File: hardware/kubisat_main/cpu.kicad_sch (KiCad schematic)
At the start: 0 parts

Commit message: added MCU based on arduino zeros ATSAMD21G18A
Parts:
- added U1: ATSAMD21G18A-A, Package_QFP:TQFP-48_7x7mm_P0.5mm, symbol MCU_Microchip_SAMD:ATSAMD21G18A-A
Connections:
- new net: U1.18 (GND), U1.35 (GND), U1.42 (GND)
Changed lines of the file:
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@@
 	(generator_version "8.0")
 	(paper "A4")
+	(symbol
+		(lib_id "MCU_Microchip_SAMD:ATSAMD21G18A-A")
+		(at 81.28 102.87 180)
+		(unit 1)
+		(exclude_from_sim no)
+		(in_bom yes)
+		(on_board yes)
+		(dnp no)
+		(fields_autoplaced yes)
+		(property "Reference" "U1"
+			(at 84.2965 52.07 0)
+			(effects
+				(font
+					(size 1.27 1.27)
+				)
+				(justify right)
+			)
+		)
+		(property "Value" "ATSAMD21G18A-A"
+			(at 84.2965 54.61 0)
+			(effects
+				(font
+					(size 1.27 1.27)
+				)
+				(justify right)
+			)
+		)
+		(property "Footprint" "Package_QFP:TQFP-48_7x7mm_P0.5mm"
+			(at 58.42 55.88 0)
+			(effects
+				(font
+					(size 1.27 1.27)
+				)
+				(hide yes)
+			)
+		)
+		(property "Datasheet" "http://ww1.microchip.com/downloads/en/DeviceDoc/SAM_D21_DA1_Family_Data%20Sheet_DS40001882E.pdf"
+			(at 81.28 128.27 0)
+			(effects
+				(font
+					(size 1.27 1.27)
+				)
+				(hide yes)
+			)
+		)
+		(property "Description" "SAM D21 Microchip SMART ARM-based Flash MCU, 48Mhz, 256K Flash, 32K SRAM, TQFP-48"
+			(at 81.28 102.87 0)
+			(effects
+				(font
+					(size 1.27 1.27)
+				)
+				(hide yes)
+			)
+		)
+		(pin "16"
+		)
+		(pin "14"
+		)
+		(pin "23"
+		)
+		(pin "45"
+		)
+		(pin "7"
+		)
+		(pin "33"
+		)
+		(pin "35"
+		)
+		(pin "46"
+		)
+		(pin "47"
+		)
+		(pin "8"
+		)
+		(pin "19"
+		)
+		(pin "2"
+		)
+		(pin "39"
+		)
+		(pin "27"
+		)
+		(pin "32"
+		)
+		(pin "44"
+		)
+		(pin "3"
+		)
+		(pin "1"
+		)
+		(pin "34"
+		)
+		(pin "40"
+		)
+		(pin "24"
+		)
+		(pin "26"
+		)
+		(pin "36"
+		)
+		(pin "18"
+		)
+		(pin "37"
+		)
+		(pin "31"
+		)
+		(pin "4"
+		)
+		(pin "20"
+		)
+		(pin "17"
+		)
+		(pin "5"
+		)
+		(pin "22"
+		)
+		(pin "28"
+		)
+		(pin "42"
+		)
+		(pin "15"
+		)
+		(pin "29"
+		)
+		(pin "6"
+		)
+		(pin "25"
+		)
+		(pin "30"
+		)
+		(pin "21"
+		)
+		(pin "48"
+		)
+		(pin "38"
+		)
+		(pin "10"
+		)
+		(pin "9"
+		)
+		(pin "41"
+		)
+		(pin "43"
+		)
+		(pin "11"
+		)
+		(pin "12"
+		)
+		(pin "13"
+		)
+		(instances
+			(project ""
+				(path "/8e012760-7134-459b-b212-1cb69dd2e1ec/2c7d03ec-a54e-4ab4-a35e-dcb69dfe6e0e"
+					(reference "U1")
+					(unit 1)
+				)
+			)
+		)
+	)
 )

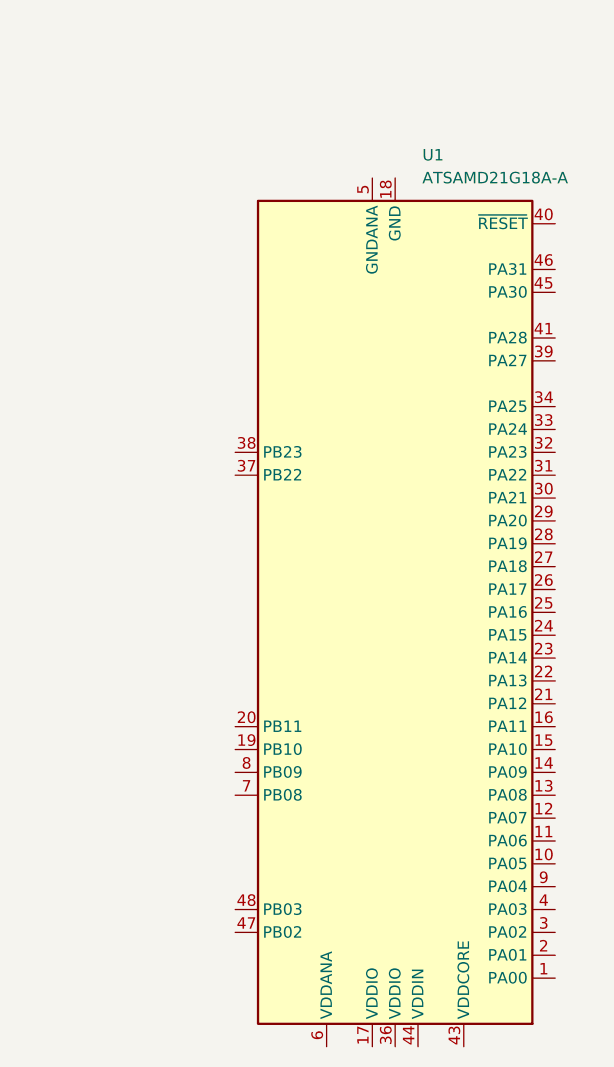
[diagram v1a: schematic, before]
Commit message: added arduino code, more items on main schematic
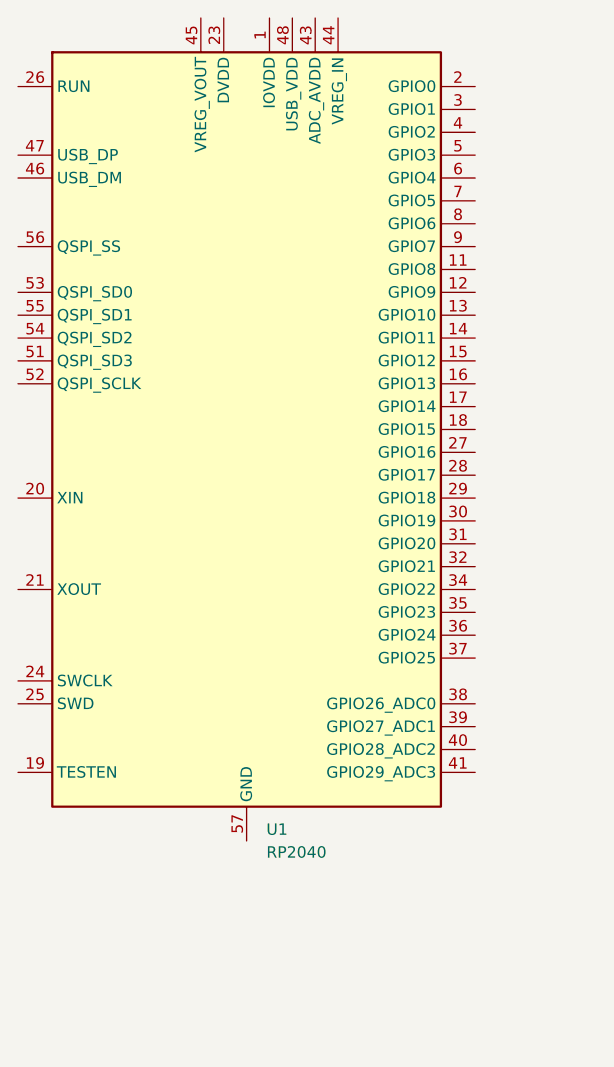
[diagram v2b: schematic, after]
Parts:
- removed U1: ATSAMD21G18A-A, Package_QFP:TQFP-48_7x7mm_P0.5mm, symbol MCU_Microchip_SAMD:ATSAMD21G18A-A
- added U1: RP2040, Package_DFN_QFN:QFN-56-1EP_7x7mm_P0.4mm_EP3.2x3.2mm, symbol MCU_RaspberryPi:RP2040
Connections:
- new net: U1.1 (IOVDD), U1.10 (IOVDD), U1.22 (IOVDD), U1.33 (IOVDD), U1.42 (IOVDD), U1.49 (IOVDD)
- new net: U1.23 (DVDD), U1.50 (DVDD)
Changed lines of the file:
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@@
 	(paper "A4")
 	(symbol
-		(lib_id "MCU_Microchip_SAMD:ATSAMD21G18A-A")
-		(at 81.28 102.87 180)
+		(lib_id "MCU_RaspberryPi:RP2040")
+		(at 64.77 82.55 0)
 		(unit 1)
 		(exclude_from_sim no)
@@
 		(fields_autoplaced yes)
 		(property "Reference" "U1"
-			(at 84.2965 52.07 0)
+			(at 66.9641 127 0)
 			(effects
 				(font
 					(size 1.27 1.27)
 				)
-				(justify right)
+				(justify left)
 			)
 		)
-		(property "Value" "ATSAMD21G18A-A"
-			(at 84.2965 54.61 0)
+		(property "Value" "RP2040"
+			(at 66.9641 129.54 0)
 			(effects
 				(font
 					(size 1.27 1.27)
 				)
-				(justify right)
+				(justify left)
 			)
 		)
-		(property "Footprint" "Package_QFP:TQFP-48_7x7mm_P0.5mm"
-			(at 58.42 55.88 0)
+		(property "Footprint" "Package_DFN_QFN:QFN-56-1EP_7x7mm_P0.4mm_EP3.2x3.2mm"
+			(at 64.77 82.55 0)
 			(effects
 				(font
@@
 			)
 		)
-		(property "Datasheet" "http://ww1.microchip.com/downloads/en/DeviceDoc/SAM_D21_DA1_Family_Data%20Sheet_DS40001882E.pdf"
-			(at 81.28 128.27 0)
+		(property "Datasheet" "https://datasheets.raspberrypi.com/rp2040/rp2040-datasheet.pdf"
+			(at 64.77 82.55 0)
 			(effects
 				(font
@@
 			)
 		)
-		(property "Description" "SAM D21 Microchip SMART ARM-based Flash MCU, 48Mhz, 256K Flash, 32K SRAM, TQFP-48"
-			(at 81.28 102.87 0)
+		(property "Description" "A microcontroller by Raspberry Pi"
+			(at 64.77 82.55 0)
 			(effects
 				(font
@@
 			)
 		)
-		(pin "16"
+		(pin "15"
 		)
 		(pin "14"
 		)
-		(pin "23"
+		(pin "25"
+		)
+		(pin "27"
+		)
+		(pin "3"
+		)
+		(pin "32"
+		)
+		(pin "1"
+		)
+		(pin "4"
+		)
+		(pin "43"
 		)
 		(pin "45"
-		)
-		(pin "7"
-		)
-		(pin "33"
-		)
-		(pin "35"
 		)
 		(pin "46"
@@
 		(pin "47"
 		)
+		(pin "53"
+		)
+		(pin "13"
+		)
+		(pin "41"
+		)
+		(pin "54"
+		)
+		(pin "30"
+		)
+		(pin "56"
+		)
+		(pin "18"
+		)
+		(pin "57"
+		)
+		(pin "36"
+		)
 		(pin "8"
+		)
+		(pin "50"
+		)
+		(pin "9"
+		)
+		(pin "16"
+		)
+		(pin "23"
+		)
+		(pin "24"
+		)
+		(pin "31"
+		)
+		(pin "44"
+		)
+		(pin "39"
+		)
+		(pin "52"
 		)
 		(pin "19"
 		)
+		(pin "38"
+		)
+		(pin "6"
+		)
+		(pin "7"
+		)
 		(pin "2"
 		)
-		(pin "39"
-		)
-		(pin "27"
-		)
-		(pin "32"
-		)
-		(pin "44"
-		)
-		(pin "3"
-		)
-		(pin "1"
+		(pin "11"
 		)
 		(pin "34"
 		)
+		(pin "42"
+		)
+		(pin "55"
+		)
+		(pin "12"
+		)
+		(pin "20"
+		)
+		(pin "28"
+		)
+		(pin "33"
+		)
+		(pin "48"
+		)
+		(pin "22"
+		)
+		(pin "49"
+		)
 		(pin "40"
 		)
-		(pin "24"
+		(pin "5"
+		)
+		(pin "51"
 		)
 		(pin "26"
 		)
-		(pin "36"
+		(pin "29"
 		)
-		(pin "18"
+		(pin "21"
+		)
+		(pin "17"
 		)
 		(pin "37"
 		)
-		(pin "31"
-		)
-		(pin "4"
-		)
-		(pin "20"
-		)
-		(pin "17"
-		)
-		(pin "5"
-		)
-		(pin "22"
-		)
-		(pin "28"
-		)
-		(pin "42"
-		)
-		(pin "15"
-		)
-		(pin "29"
-		)
-		(pin "6"
-		)
-		(pin "25"
-		)
-		(pin "30"
-		)
-		(pin "21"
-		)
-		(pin "48"
-		)
-		(pin "38"
+		(pin "35"
 		)
 		(pin "10"
 		)
-		(pin "9"
-		)
-		(pin "41"
-		)
-		(pin "43"
-		)
-		(pin "11"
-		)
-		(pin "12"
-		)
-		(pin "13"
-		)
 		(instances

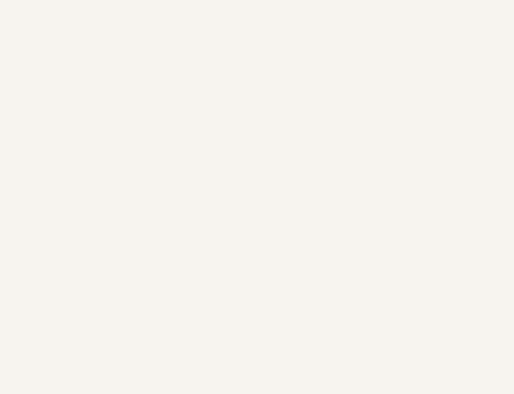
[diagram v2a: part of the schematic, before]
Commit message: added elements and traces to main pcb
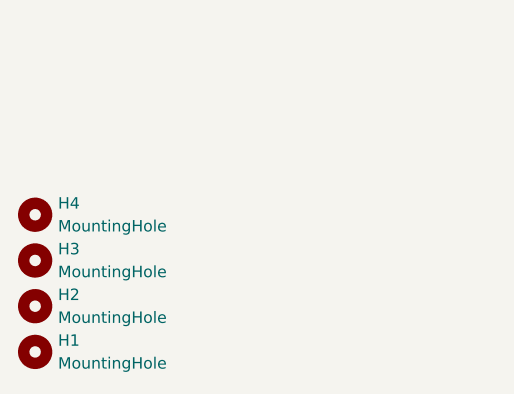
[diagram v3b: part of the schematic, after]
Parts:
- added H1, H2, H3, H4: MountingHole, MountingHole:MountingHole_3.2mm_M3_DIN965, symbol Mechanical:MountingHole

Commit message: added microsd footprint
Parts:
- removed U1: RP2040, Package_DFN_QFN:QFN-56-1EP_7x7mm_P0.4mm_EP3.2x3.2mm, symbol MCU_RaspberryPi:RP2040
- added J2: Micro_SD_Card_Det1, Connector_Card:MR01A-01211, symbol Connector:Micro_SD_Card_Det1
- added J3, J4: Conn_01x08_Socket, Connector_PinHeader_2.54mm:PinHeader_1x08_P2.54mm_Vertical, symbol Connector:Conn_01x08_Socket
- added J5: Conn_01x07_Socket, Connector_PinSocket_2.54mm:PinSocket_1x07_P2.54mm_Vertical, symbol Connector:Conn_01x07_Socket

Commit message: added elements to cpu schematic
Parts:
- removed J3, J4: Conn_01x08_Socket, Connector_PinHeader_2.54mm:PinHeader_1x08_P2.54mm_Vertical, symbol Connector:Conn_01x08_Socket
- removed J5: Conn_01x07_Socket, Connector_PinSocket_2.54mm:PinSocket_1x07_P2.54mm_Vertical, symbol Connector:Conn_01x07_Socket
- added C11, C12, C14, C18, C19, C20, C21, C22, C23, C24, C25: 100n, Capacitor_SMD:C_0805_2012Metric, symbol Device:C
- added C13, C15: 2u2, Capacitor_SMD:C_0805_2012Metric, symbol Device:C
- added C16, C17: 15p, Capacitor_SMD:C_0805_2012Metric, symbol Device:C
- added J3: Conn_01x06_MountingPin, Connector_JST:JST_PH_S6B-PH-SM4-TB_1x06-1MP_P2.00mm_Horizontal, symbol Connector_Generic_MountingPin:Conn_01x06_MountingPin
- added R10, R11, R14: 27, symbol Device:R
- added R12: 1, symbol Device:R
- added R13: 200, symbol Device:R
- added R15: 1k, symbol Device:R
- added SW1: BOOTSEL, Button_Switch_SMD:SW_MEC_5GSH9, symbol Switch:SW_Push
- added SW2: RESET, Button_Switch_SMD:SW_MEC_5GSH9, symbol Switch:SW_Push
- added U1: RP2040, Package_DFN_QFN:QFN-56-1EP_7x7mm_P0.4mm_EP3.2x3.2mm, symbol MCU_RaspberryPi:RP2040
- added U6: W25Q16JVSS, Package_SO:SOIC-8_5.23x5.23mm_P1.27mm, symbol Memory_Flash:W25Q16JVSS
- added Y1: 12MHz, Crystal:Crystal_SMD_3225-4Pin_3.2x2.5mm, symbol Device:Crystal_GND24
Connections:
- new net: C13.2, R12.1, U1.43 (ADC_AVDD)
- new net: R12.2, R13.2
- new net: R15.2, SW1.2
- new net: C17.2, R14.1, Y1.3
- new net: R14.2, U1.21 (XOUT)
- new net: C16.2, U1.20 (XIN), Y1.1
- new net: SW2.2, U1.26 (RUN)
- new net: U1.51 (QSPI_SD3), U6.7 (IO3)
- new net: U1.52 (QSPI_SCLK), U6.6 (CLK)
- new net: U1.53 (QSPI_SD0), U6.5 (DI(IO0))
- new net: U1.54 (QSPI_SD2), U6.3 (IO2)
- new net: U1.55 (QSPI_SD1), U6.2 (DO(IO1))
- new net: R15.1, U1.56 (QSPI_SS), U6.1 (~{CS})
- new net +1V1: C11.1, C12.2, C25.2, U1.23 (DVDD), U1.45 (VREG_VOUT), U1.50 (DVDD)
- new net +3V3: C14.2, C15.2, C18.1, C19.1, C20.1, C21.1, C22.1, C23.1, C24.1, R13.1, U1.1 (IOVDD), U1.10 (IOVDD), U1.22 (IOVDD), U1.33 (IOVDD), U1.42 (IOVDD), U1.44 (VREG_IN), U1.48 (USB_VDD), U1.49 (IOVDD), U6.8 (VCC)
- new net GND: C11.2, C12.1, C13.1, C14.1, C15.1, C16.1, C17.1, C18.2, C19.2, C20.2, C21.2, C22.2, C23.2, C24.2, C25.1, SW1.1, SW2.1, U1.19 (TESTEN), U1.57 (GND), U6.4 (GND), Y1.2, Y1.4
- new net I2C0_SCL: U1.7 (GPIO5)
- new net I2C0_SDA: U1.6 (GPIO4)
- new net SX1278.MISO: U1.27 (GPIO16)
- new net SX1278.MOSI: U1.30 (GPIO19)
- new net SX1278.NSS: U1.28 (GPIO17)
- new net SX1278.SCLK: U1.29 (GPIO18)
- new net UART0_RX: U1.3 (GPIO1)
- new net UART0_TX: U1.2 (GPIO0)
- new net USB_DM: U1.46 (USB_DM)
- new net USB_DP: U1.47 (USB_DP)
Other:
- moved on the sheet: H1, H2, H3, H4, J2

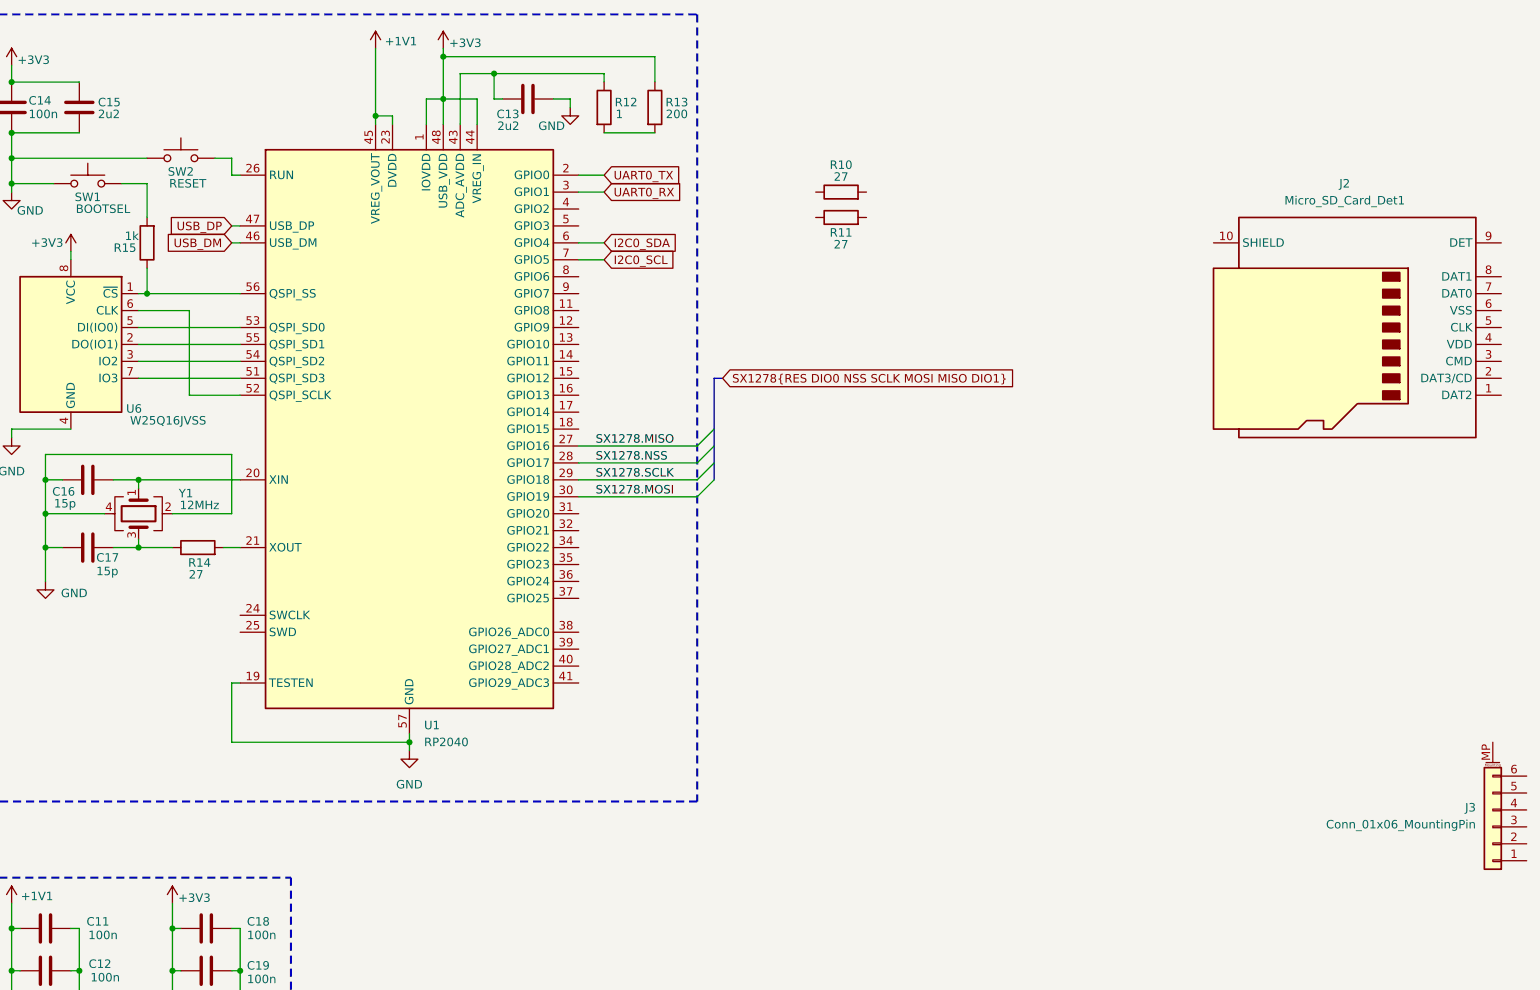
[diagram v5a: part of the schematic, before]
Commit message: added pcb elements
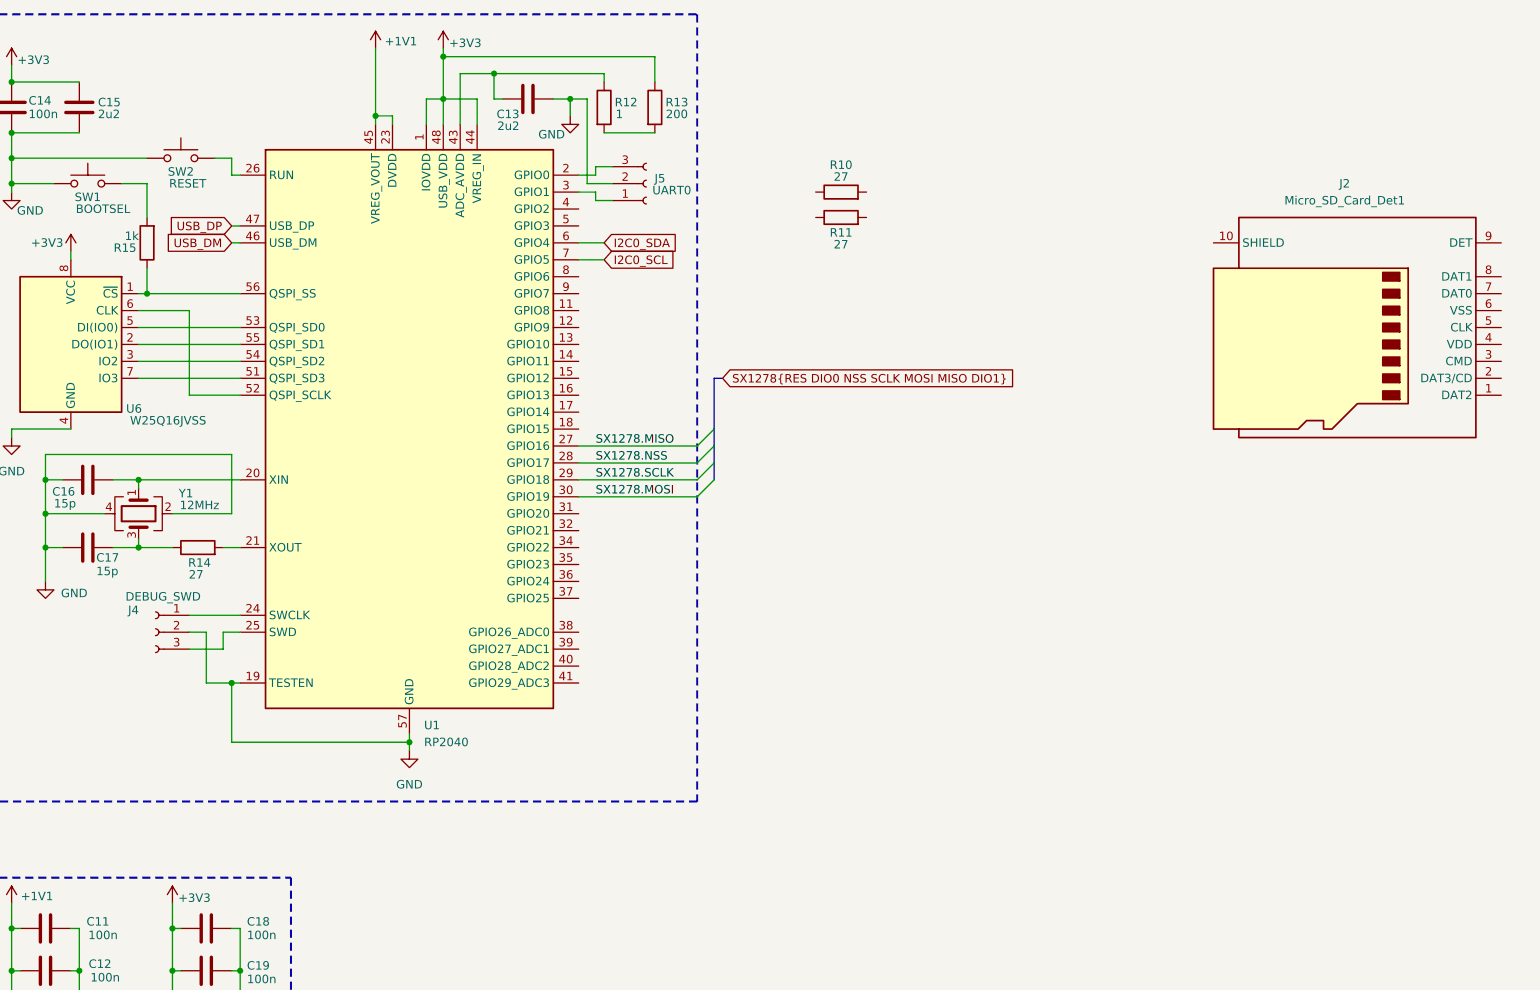
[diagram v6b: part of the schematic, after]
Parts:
- removed J3: Conn_01x06_MountingPin, Connector_JST:JST_PH_S6B-PH-SM4-TB_1x06-1MP_P2.00mm_Horizontal, symbol Connector_Generic_MountingPin:Conn_01x06_MountingPin
- added J4: DEBUG_SWD, Connector_PinHeader_1.00mm:PinHeader_1x03_P1.00mm_Vertical, symbol Connector:Conn_01x03_Socket
- added J5: UART0, Connector_PinHeader_1.00mm:PinHeader_1x03_P1.00mm_Vertical, symbol Connector:Conn_01x03_Socket
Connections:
- net GND: now also J4.2 (Pin_2), J5.2 (Pin_2)
- net at U1.24 (SWCLK): now also J4.1 (Pin_1)
- net at U1.25 (SWD): now also J4.3 (Pin_3)
- net UART0_RX: no longer names the net of U1.3 (GPIO1)
- net UART0_RX: now also J5.1 (Pin_1)
- net UART0_TX: no longer names the net of U1.2 (GPIO0)
- net UART0_TX: now also J5.3 (Pin_3)
